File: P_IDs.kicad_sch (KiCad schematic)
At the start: 0 parts

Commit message: added igniter
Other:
- added sheet Igniter Test (IgniterTest.kicad_sch)
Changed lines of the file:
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@@
 	(paper "A4")
+	(sheet
+		(at 204.978 34.036)
+		(size 44.45 19.812)
+		(fields_autoplaced yes)
+		(stroke
+			(width 0.1524)
+			(type solid)
+		)
+		(fill
+			(color 0 0 0 0.0000)
+		)
+		(property "Sheetname" "Igniter Test"
+			(at 204.978 33.3244 0)
+			(effects
+				(font
+					(size 1.27 1.27)
+				)
+				(justify left bottom)
+			)
+		)
+		(property "Sheetfile" "IgniterTest.kicad_sch"
+			(at 204.978 54.4326 0)
+			(effects
+				(font
+					(size 1.27 1.27)
+				)
+				(justify left top)
+			)
+		)
+		(instances
+			(project "P_IDs"
+				(path "/045f1f05-3134-4b6d-91b6-463031104f1e"
+					(page "4")
+				)
+			)
+		)
+	)
 	(sheet
 		(at 132.08 33.02)

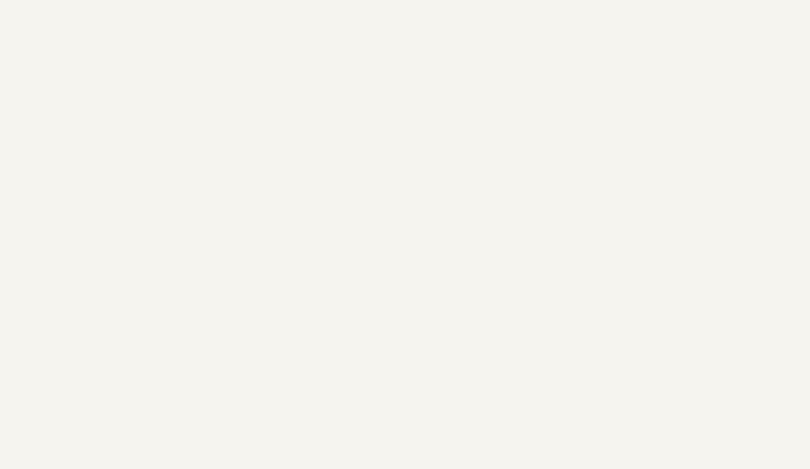
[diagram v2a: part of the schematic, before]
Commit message: added answer key and gitignore
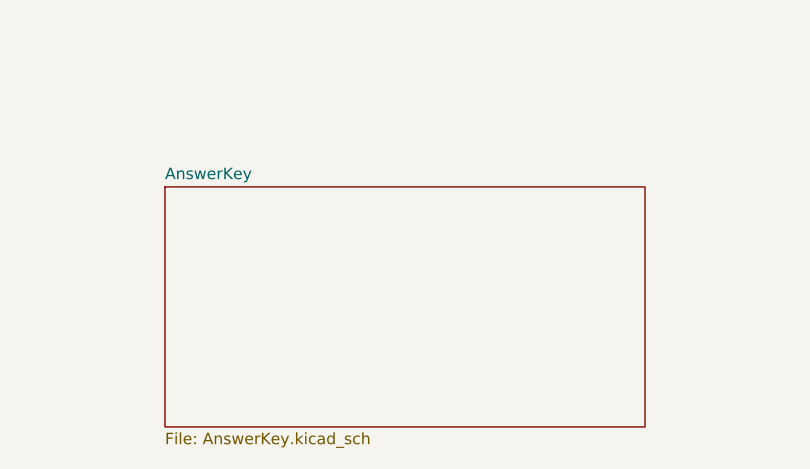
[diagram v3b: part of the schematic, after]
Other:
- added sheet AnswerKey (AnswerKey.kicad_sch)
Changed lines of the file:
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@@
+	)
+	(sheet
+		(at 139.7 83.82)
+		(size 53.34 26.67)
+		(fields_autoplaced yes)
+		(stroke
+			(width 0.1524)
+			(type solid)
+		)
+		(fill
+			(color 0 0 0 0.0000)
+		)
+		(property "Sheetname" "AnswerKey"
+			(at 139.7 83.1084 0)
+			(effects
+				(font
+					(size 1.27 1.27)
+				)
+				(justify left bottom)
+			)
+		)
+		(property "Sheetfile" "AnswerKey.kicad_sch"
+			(at 139.7 111.0746 0)
+			(effects
+				(font
+					(size 1.27 1.27)
+				)
+				(justify left top)
+			)
+		)
+		(instances
+			(project "P_IDs"
+				(path "/045f1f05-3134-4b6d-91b6-463031104f1e"
+					(page "5")
+				)
+			)
+		)
 	)
 	(sheet

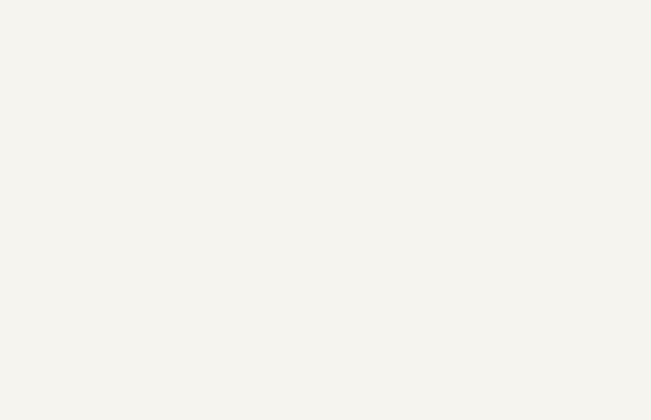
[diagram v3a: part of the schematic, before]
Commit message: added hotfire P&ID setup
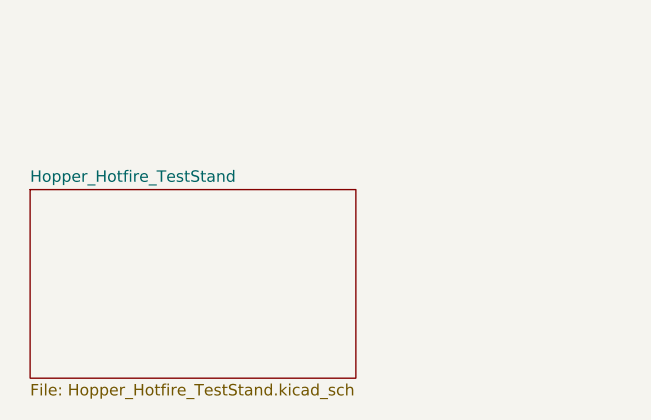
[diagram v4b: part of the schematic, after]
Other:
- added sheet Hopper_Hotfire_TestStand (Hopper_Hotfire_TestStand.kicad_sch)
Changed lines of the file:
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@@
 	(paper "A4")
+	(sheet
+		(at 57.15 93.345)
+		(size 36.195 20.955)
+		(fields_autoplaced yes)
+		(stroke
+			(width 0.1524)
+			(type solid)
+		)
+		(fill
+			(color 0 0 0 0.0000)
+		)
+		(property "Sheetname" "Hopper_Hotfire_TestStand"
+			(at 57.15 92.6334 0)
+			(effects
+				(font
+					(size 1.27 1.27)
+				)
+				(justify left bottom)
+			)
+		)
+		(property "Sheetfile" "Hopper_Hotfire_TestStand.kicad_sch"
+			(at 57.15 114.8846 0)
+			(effects
+				(font
+					(size 1.27 1.27)
+				)
+				(justify left top)
+			)
+		)
+		(instances
+			(project "P_IDs"
+				(path "/045f1f05-3134-4b6d-91b6-463031104f1e"
+					(page "6")
+				)
+			)
+		)
+	)
 	(sheet
 		(at 204.978 34.036)

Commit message: camebackfromhol
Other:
- removed sheet Skywalker
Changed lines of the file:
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@@
-		)
-	)
-	(sheet
-		(at 55.88 34.29)
-		(size 46.99 24.13)
-		(fields_autoplaced yes)
-		(stroke
-			(width 0.1524)
-			(type solid)
-		)
-		(fill
-			(color 0 0 0 0.0000)
-		)
-		(property "Sheetname" "Skywalker"
-			(at 55.88 33.5784 0)
-			(effects
-				(font
-					(size 1.27 1.27)
-				)
-				(justify left bottom)
-			)
-		)
-		(property "Sheetfile" "Skywalker.kicad_sch"
-			(at 55.88 59.0046 0)
-			(effects
-				(font
-					(size 1.27 1.27)
-				)
-				(justify left top)
-			)
-		)
-		(instances
-			(project "P_IDs"
-				(path "/045f1f05-3134-4b6d-91b6-463031104f1e"
-					(page "2")
-				)
-			)
 		)
 	)

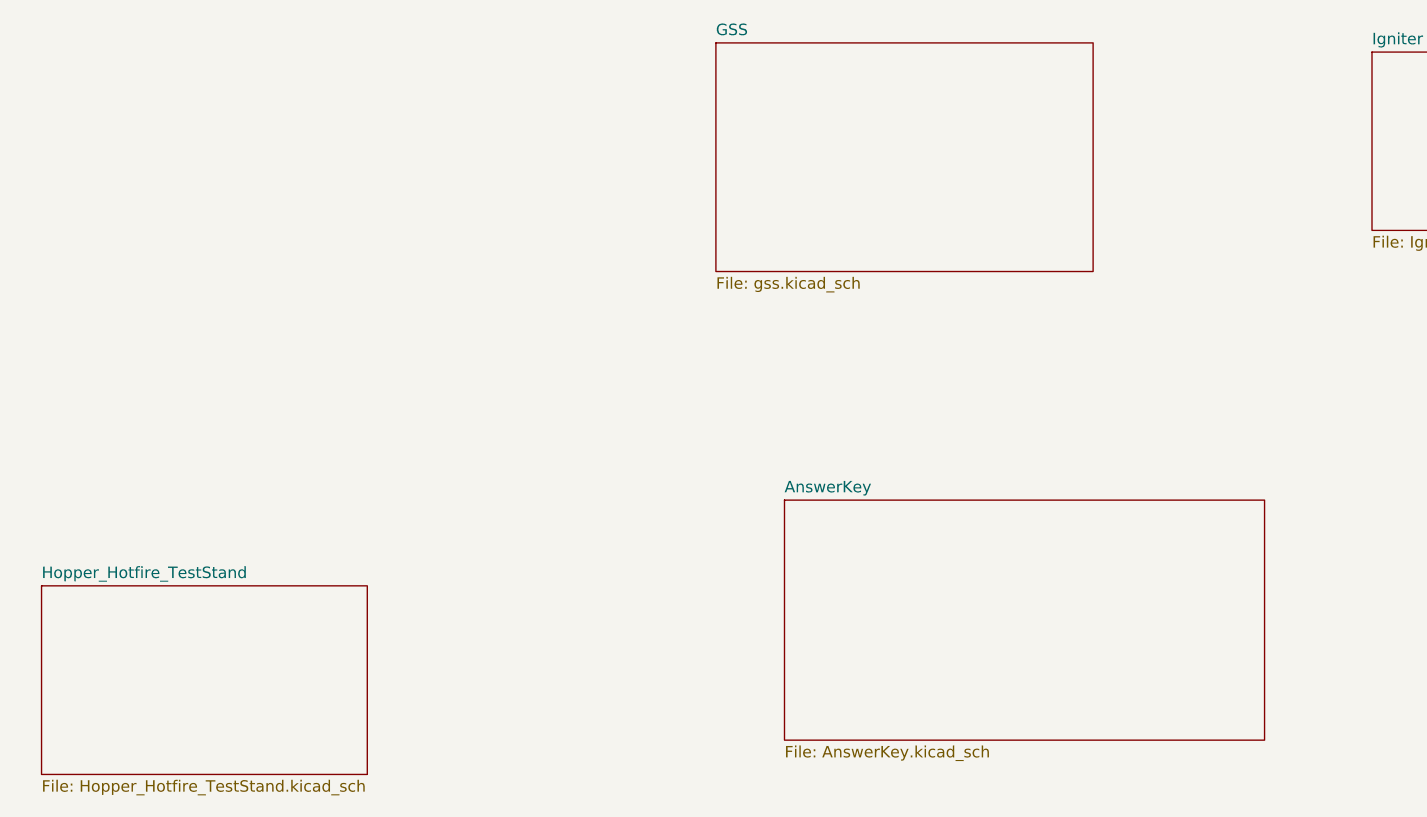
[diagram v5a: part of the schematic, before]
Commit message: deleted answer keys
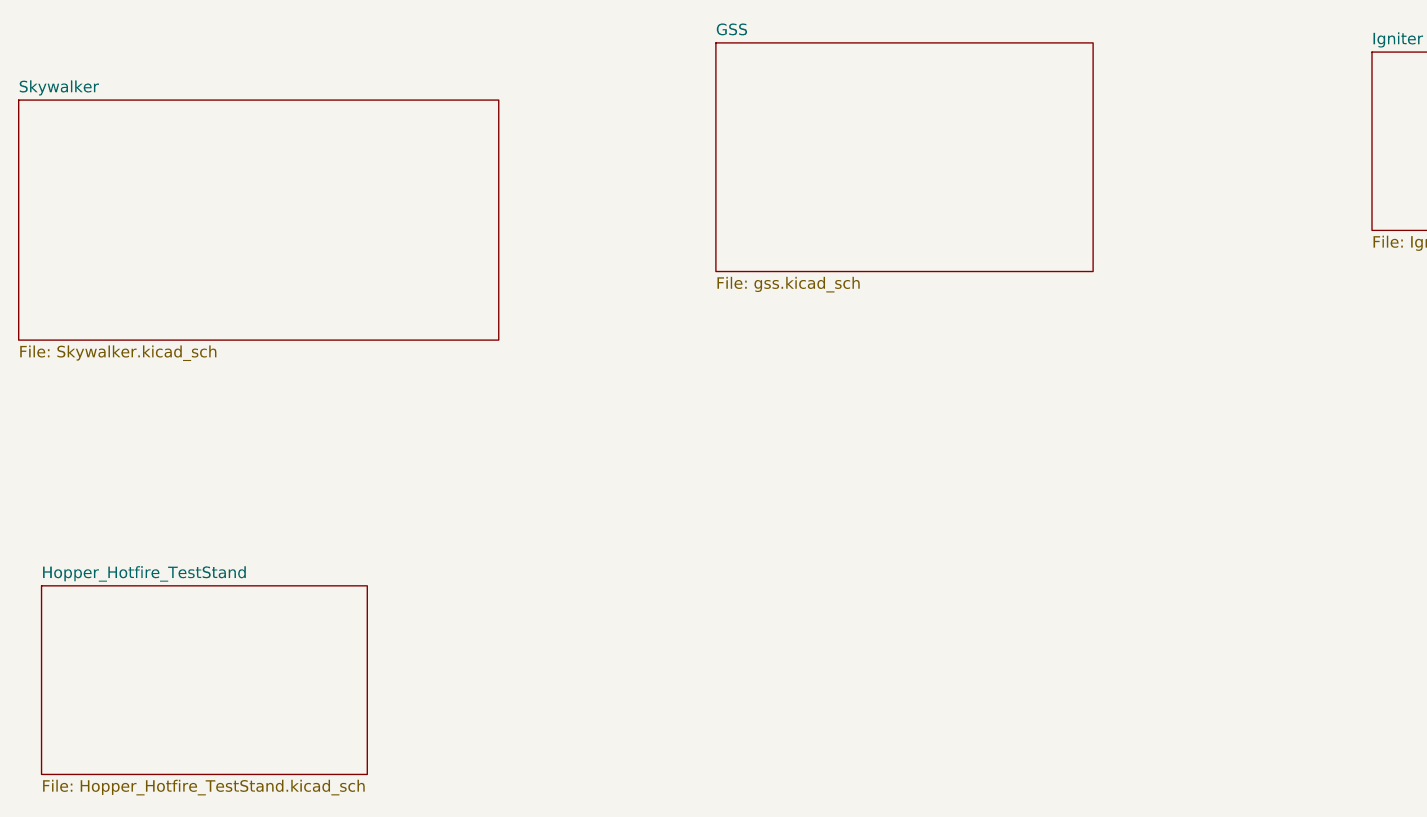
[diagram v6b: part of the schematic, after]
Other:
- sheet AnswerKey renamed Skywalker
- sheet Skywalker: file AnswerKey.kicad_sch -> Skywalker.kicad_sch
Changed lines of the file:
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@@
 	)
 	(sheet
-		(at 139.7 83.82)
+		(at 54.61 39.37)
 		(size 53.34 26.67)
 		(fields_autoplaced yes)
@@
 			(color 0 0 0 0.0000)
 		)
-		(property "Sheetname" "AnswerKey"
-			(at 139.7 83.1084 0)
+		(property "Sheetname" "Skywalker"
+			(at 54.61 38.6584 0)
 			(effects
 				(font
@@
 			)
 		)
-		(property "Sheetfile" "AnswerKey.kicad_sch"
-			(at 139.7 111.0746 0)
+		(property "Sheetfile" "Skywalker.kicad_sch"
+			(at 54.61 66.6246 0)
 			(effects
 				(font
@@
 			)
 		)
+		(property "Field2" ""
+			(at 54.61 39.37 0)
+			(effects
+				(font
+					(size 1.27 1.27)
+				)
+				(hide yes)
+			)
+		)

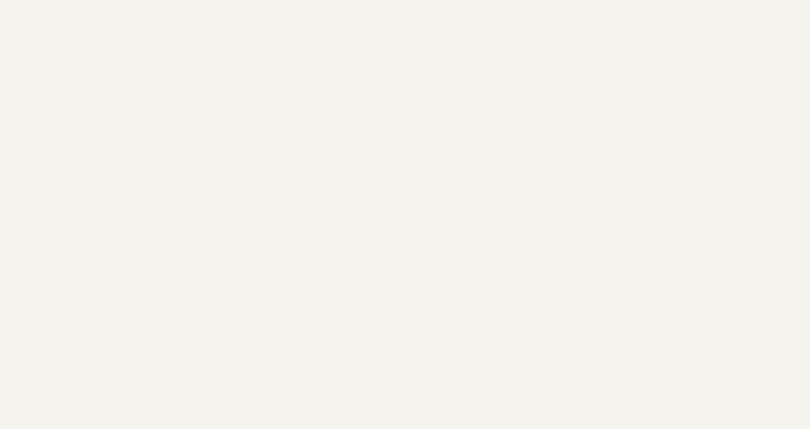
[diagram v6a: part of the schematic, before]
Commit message: added L9 P&ID from Babs, he had problems using git
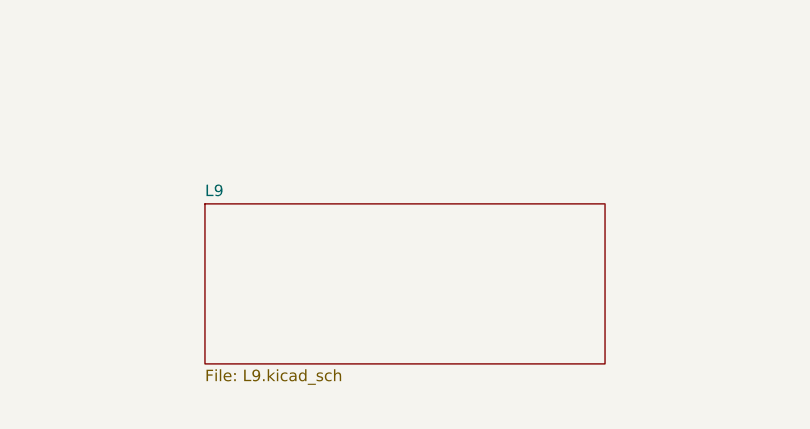
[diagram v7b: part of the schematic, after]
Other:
- added sheet L9 (L9.kicad_sch)
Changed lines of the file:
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@@
+	)
+	(sheet
+		(at 160.02 93.98)
+		(size 44.45 17.78)
+		(fields_autoplaced yes)
+		(stroke
+			(width 0.1524)
+			(type solid)
+		)
+		(fill
+			(color 0 0 0 0.0000)
+		)
+		(property "Sheetname" "L9"
+			(at 160.02 93.2684 0)
+			(effects
+				(font
+					(size 1.27 1.27)
+				)
+				(justify left bottom)
+			)
+		)
+		(property "Sheetfile" "L9.kicad_sch"
+			(at 160.02 112.3446 0)
+			(effects
+				(font
+					(size 1.27 1.27)
+				)
+				(justify left top)
+			)
+		)
+		(instances
+			(project "P_IDs"
+				(path "/045f1f05-3134-4b6d-91b6-463031104f1e"
+					(page "6")
+				)
+			)
+		)
 	)
 	(sheet

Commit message: igniter+hotfire
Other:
- added sheet Skywalker Engine + Igniter Test (skywalkerEngine+IgniterTest.kicad_sch)
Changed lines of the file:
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@@
 	(paper "A4")
 	(sheet
-		(at 57.15 93.345)
-		(size 36.195 20.955)
+		(at 127 18.415)
+		(size 41.91 24.765)
 		(fields_autoplaced yes)
 		(stroke
@@
 		)
 		(property "Sheetname" "Hopper_Hotfire_TestStand"
-			(at 57.15 92.6334 0)
+			(at 127 17.7034 0)
 			(effects
 				(font
@@
 		)
 		(property "Sheetfile" "Hopper_Hotfire_TestStand.kicad_sch"
-			(at 57.15 114.8846 0)
+			(at 127 43.7646 0)
 			(effects
 				(font
@@
 	)
 	(sheet
-		(at 204.978 34.036)
-		(size 44.45 19.812)
+		(at 127 52.07)
+		(size 41.91 24.13)
 		(fields_autoplaced yes)
 		(stroke
@@
 		)
 		(property "Sheetname" "Igniter Test"
-			(at 204.978 33.3244 0)
+			(at 127 51.3584 0)
 			(effects
 				(font
@@
 		)
 		(property "Sheetfile" "IgniterTest.kicad_sch"
-			(at 204.978 54.4326 0)
+			(at 127 76.7846 0)
 			(effects
 				(font
@@
 	)
 	(sheet
-		(at 160.02 93.98)
-		(size 44.45 17.78)
+		(at 17.78 106.68)
+		(size 215.9 45.72)
 		(fields_autoplaced yes)
 		(stroke
@@
 		)
 		(property "Sheetname" "L9"
-			(at 160.02 93.2684 0)
+			(at 17.78 105.9684 0)
 			(effects
 				(font
@@
 		)
 		(property "Sheetfile" "L9.kicad_sch"
-			(at 160.02 112.3446 0)
+			(at 17.78 152.9846 0)
 			(effects
 				(font
@@
 	)
 	(sheet
-		(at 54.61 39.37)
-		(size 53.34 26.67)
+		(at 16.51 16.51)
+		(size 104.14 60.96)
 		(fields_autoplaced yes)
 		(stroke
@@
 		)
 		(property "Sheetname" "Skywalker"
-			(at 54.61 38.6584 0)
+			(at 16.51 15.7984 0)
 			(effects
 				(font
@@
 		)
 		(property "Sheetfile" "Skywalker.kicad_sch"
-			(at 54.61 66.6246 0)
+			(at 16.51 78.0546 0)
 			(effects
 				(font
@@
 		)
 		(property "Field2" ""
-			(at 54.61 39.37 0)
+			(at 16.51 16.51 0)
 			(effects
 				(font
@@
 	)
 	(sheet
-		(at 132.08 33.02)
-		(size 41.91 25.4)
+		(at 237.49 17.78)
+		(size 41.91 134.62)
 		(fields_autoplaced yes)
 		(stroke
@@
 		)
 		(property "Sheetname" "GSS"
-			(at 132.08 32.3084 0)
+			(at 237.49 17.0684 0)
 			(effects
 				(font
@@
 		)
 		(property "Sheetfile" "gss.kicad_sch"
-			(at 132.08 59.0046 0)
+			(at 237.49 152.9846 0)
 			(effects
 				(font
@@
 				)
 			)
+		)
+	)
+	(sheet
+		(at 172.72 17.78)
+		(size 60.96 58.42)
+		(fields_autoplaced yes)
+		(stroke
+			(width 0.1524)
+			(type solid)
+		)
+		(fill
+			(color 0 0 0 0.0000)
+		)
+		(property "Sheetname" "Skywalker Engine + Igniter Test"
+			(at 172.72 17.0684 0)
+			(effects
+				(font
+					(size 1.27 1.27)
+				)
+				(justify left bottom)
+			)
+		)
+		(property "Sheetfile" "skywalkerEngine+IgniterTest.kicad_sch"
+			(at 172.72 76.7846 0)
+			(effects
+				(font
+					(size 1.27 1.27)
+				)
+				(justify left top)
+			)
+		)
+		(instances
+			(project "P_IDs"
+				(path "/045f1f05-3134-4b6d-91b6-463031104f1e"
+					(page "7")
+				)
+			)
